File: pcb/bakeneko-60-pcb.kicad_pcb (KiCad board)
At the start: 2 copper layers, 284.7 x 94.2 mm, 151 parts, among them J1 JST SH 4-pin, J2 AVR-ISP-6, SW1 Reset, U1 SRV05-4, U2 ATmega32U4-AU, Y1 16MHz

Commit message: Update name/version
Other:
- board text added: "Unbakeneko60 v0.1"
- board text removed: "Bakeneko60 v3.0"
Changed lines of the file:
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@@
   (gr_line (start 284.7 91.95) (end 284.7 2.25) (layer "Edge.Cuts") (width 0.2))
   (gr_arc (start 249.918072 0.806452) (mid 250.470392 0.217362) (end 251.248106 0) (layer "Edge.Cuts") (width 0.2))
-  (gr_text "Bakeneko60 v3.0" (at 274.915477 91.907501) (layer "B.SilkS")
+  (gr_text "Unbakeneko60 v0.1" (at 274.915477 91.907501) (layer "B.SilkS")
     (effects (font (size 1 1) (thickness 0.15)) (justify mirror))
   )

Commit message: Renumbering and cleanup
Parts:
- added D59: 1N4148, Diode_SMD:D_SOD-123, B.Cu at (82.8, 86.0)
- added D60: 1N4148, Diode_SMD:D_SOD-123, B.Cu at (116.1, 86.0)
- added D61: 1N4148, Diode_SMD:D_SOD-123, B.Cu at (154.3, 86.0)
- renumbered D60 to D62, D61 to D63, D62 to D64, D63 to D65
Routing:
- net Net-(D58-Pad2): track 6.82 -> 27.3 mm
- net COL11: track 295.1 -> 292.8 mm

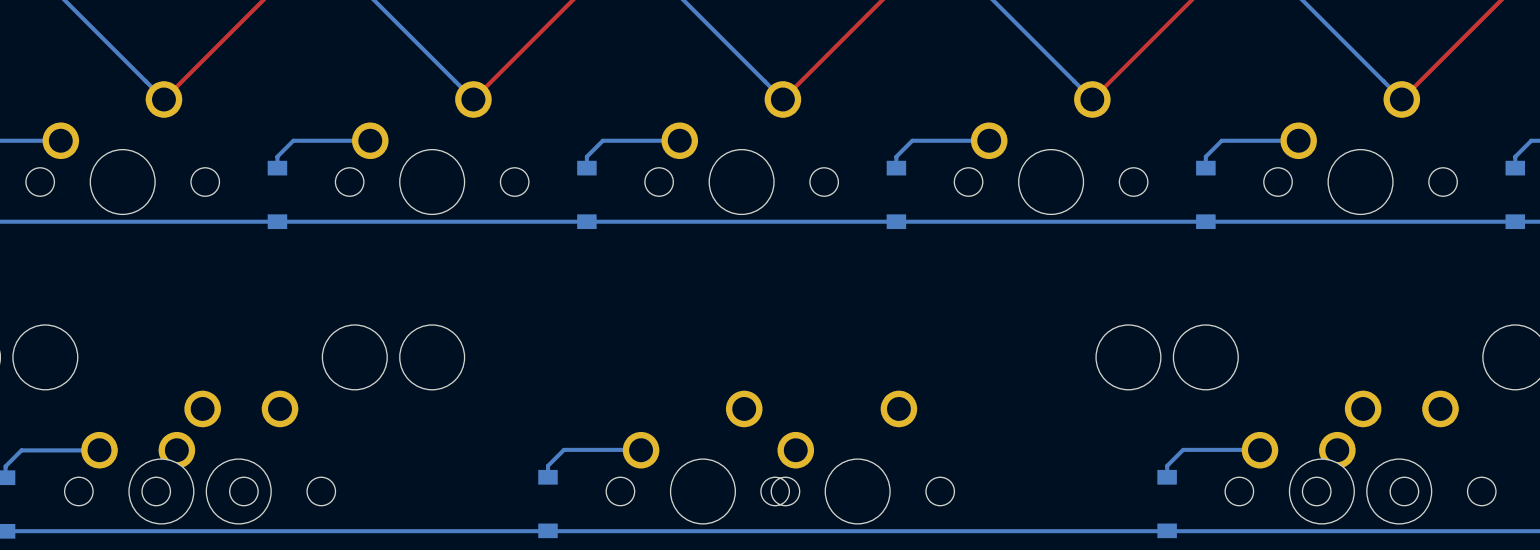
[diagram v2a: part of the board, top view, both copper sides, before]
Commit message: Add remaining traces
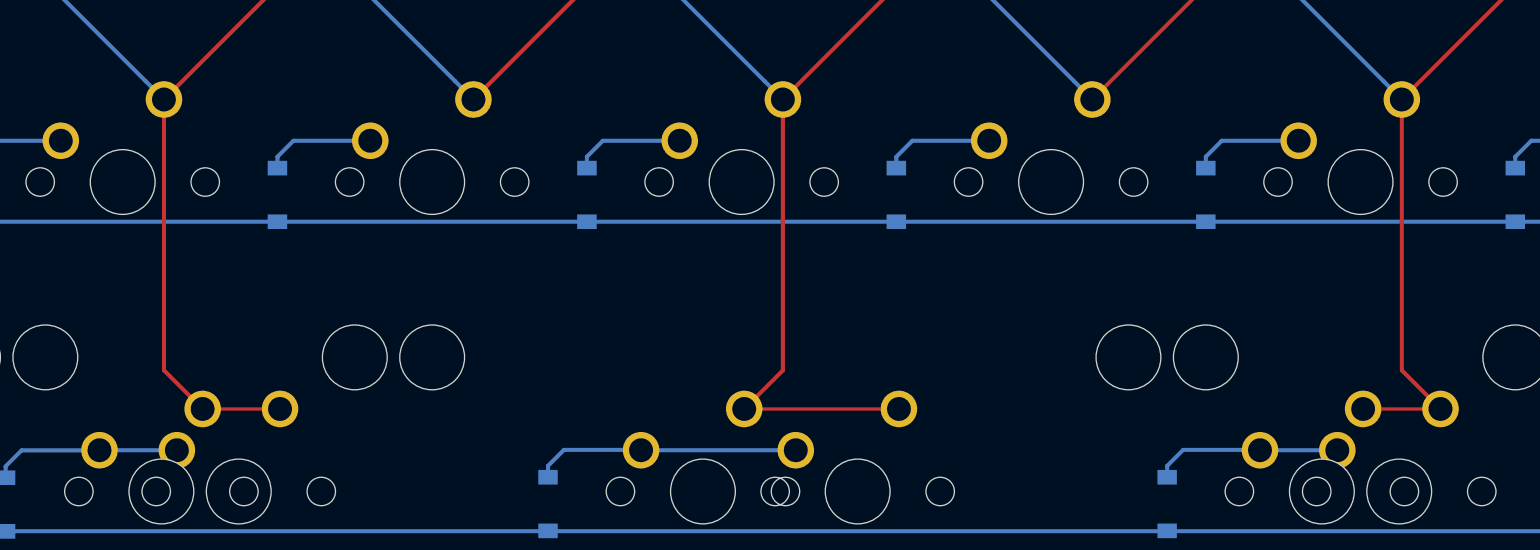
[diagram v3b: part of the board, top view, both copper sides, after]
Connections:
- D59 pad 2: Net-(D58-Pad2) -> Net-(D59-Pad2)
- D60 pad 2: Net-(D58-Pad2) -> Net-(D60-Pad2)
- D61 pad 2: Net-(D58-Pad2) -> Net-(D61-Pad2)
- MX62 pad 1: (no net) -> Net-(D59-Pad2)
- MX62 pad 2: (no net) -> COL4
- MX63 pad 2: (no net) -> COL4
- MX64 pad 1: (no net) -> Net-(D60-Pad2)
- MX64 pad 2: (no net) -> COL6
- MX65 pad 2: (no net) -> COL6
- MX66 pad 1: (no net) -> Net-(D61-Pad2)
- MX66 pad 2: (no net) -> COL8
- MX67 pad 1: (no net) -> Net-(D61-Pad2)
- MX67 pad 2: (no net) -> COL8
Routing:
- net COL6: track 180.1 -> 209.7 mm
- net COL8: track 217.4 -> 242.2 mm
- net COL4: track 143.4 -> 168.2 mm
- net Net-(D58-Pad2): track 27.3 -> 6.82 mm
- net Net-(D60-Pad2): track 0.00 -> 16.3 mm
- net Net-(D59-Pad2): track 0.00 -> 11.6 mm
- net Net-(D61-Pad2): track 0.00 -> 11.6 mm

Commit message: Remove unconnected traces
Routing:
- net COL2: track 145.1 -> 144.2 mm
- net +5V: track 122.7 -> 121.9 mm
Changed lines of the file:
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@@
   (segment (start 22.85375 37.75875) (end 21.85375 37.75875) (width 0.25) (layer "B.Cu") (net 54))
   (segment (start 21.85375 37.75875) (end 20.508769 36.413769) (width 0.25) (layer "B.Cu") (net 54))
-  (segment (start 266.1375 68.59375) (end 266.14375 68.6) (width 0.25) (layer "B.Cu") (net 54))
   (segment (start 28.84375 68.59375) (end 266.1375 68.59375) (width 0.25) (layer "B.Cu") (net 54))
   (segment (start 119.52125 63.61) (end 118.5375 64.59375) (width 0.25) (layer "B.Cu") (net 55))
@@
   (segment (start 45.1 17) (end 44.225 17) (width 0.2) (layer "B.Cu") (net 73))
   (segment (start 41.540001 17.275) (end 43.85 17.275) (width 0.2) (layer "B.Cu") (net 73))
-  (segment (start 24.80375 14.040002) (end 24.82375 14.020002) (width 0.25) (layer "F.Cu") (net 74))
   (segment (start 24.71 20.922661) (end 24.71 14.020002) (width 0.25) (layer "F.Cu") (net 74))
   (segment (start 31.902295 22.228536) (end 31.403751 21.729992) (width 0.25) (layer "F.Cu") (net 74))
@@
   (segment (start 23.100031 13.660033) (end 14.175959 13.660033) (width 0.25) (layer "B.Cu") (net 75))
   (segment (start 25.20375 14.78) (end 25.560001 14.423749) (width 0.25) (layer "F.Cu") (net 76))
-  (segment (start 33.152295 23.252418) (end 33.15375 23.250963) (width 0.25) (layer "F.Cu") (net 76))
   (segment (start 33.152295 21.928545) (end 32.503731 21.279981) (width 0.25) (layer "F.Cu") (net 76))
   (segment (start 32.503731 21.279981) (end 25.703731 21.279981) (width 0.25) (layer "F.Cu") (net 76))
@@
   (segment (start 13.92125 42.02) (end 13.92125 38.638765) (width 0.25) (layer "F.Cu") (net 77))
   (segment (start 24.643741 59.872509) (end 24.643741 51.179221) (width 0.25) (layer "F.Cu") (net 77))
-  (segment (start 15.58224 80.05) (end 15.68734 80.05) (width 0.25) (layer "F.Cu") (net 77))
   (segment (start 22.684345 46.020595) (end 22.684345 47.640595) (width 0.25) (layer "F.Cu") (net 77))
   (segment (start 13.92125 38.638765) (end 16.3025 36.257515) (width 0.25) (layer "F.Cu") (net 77))
-  (segment (start 15.51224 80.12) (end 15.58224 80.05) (width 0.25) (layer "F.Cu") (net 77))
   (segment (start 23.44625 61.07) (end 24.643741 59.872509) (width 0.25) (layer "F.Cu") (net 77))
   (segment (start 18.68375 42.02) (end 22.684345 46.020595) (width 0.25) (layer "F.Cu") (net 77))
@@
   (segment (start 39.295 22.15) (end 40.115 22.97) (width 0.25) (layer "B.Cu") (net 78))
   (segment (start 30.15375 32.05875) (end 30.15375 29.60298) (width 0.25) (layer "B.Cu") (net 78))
-  (segment (start 21.23377 36.96593) (end 21.23377 37.34002) (width 0.25) (layer "F.Cu") (net 79))
   (segment (start 26.24875 49.95) (end 25.32375 49.95) (width 0.25) (layer "F.Cu") (net 79))
   (segment (start 49.64 3.92) (end 49.64 13.445) (width 0.25) (layer "F.Cu") (net 79))
@@
   (segment (start 26.24875 49.95) (end 26.645716 49.95) (width 0.25) (layer "B.Cu") (net 79))
   (segment (start 49.051383 55.718883) (end 49.501389 56.168889) (width 0.25) (layer "B.Cu") (net 79))
-  (segment (start 35.29375 55.72) (end 35.86375 55.72) (width 0.25) (layer "B.Cu") (net 79))
   (segment (start 22.85375 36.95875) (end 21.85375 36.95875) (width 0.25) (layer "B.Cu") (net 79))
   (segment (start 29.908317 53.212605) (end 32.786355 53.212605) (width 0.25) (layer "B.Cu") (net 79))
@@
   (segment (start 16.23625 39.35875) (end 16.6475 39.77) (width 0.381) (layer "B.Cu") (net 94))
   (segment (start 38.179381 31.459383) (end 37.779382 31.859382) (width 0.381) (layer "B.Cu") (net 94))
-  (segment (start 12.604391 15.960641) (end 12.804524 15.760509) (width 0.381) (layer "B.Cu") (net 94))
   (segment (start 36.36 32.9825) (end 36.05551 33.28699) (width 0.381) (layer "B.Cu") (net 94))
   (segment (start 14.366043 14.198989) (end 21.388989 14.198989) (width 0.381) (layer "B.Cu") (net 94))
   (segment (start 12.604391 15.960641) (end 14.366043 14.198989) (width 0.381) (layer "B.Cu") (net 94))
   (segment (start 31.1225 48.2575) (end 31.12 48.26) (width 0.381) (layer "B.Cu") (net 94))
-  (segment (start 31.853749 43.558749) (end 31.75375 43.45875) (width 0.381) (layer "B.Cu") (net 94))
   (segment (start 35.180291 35.35875) (end 34.25375 35.35875) (width 0.381) (layer "B.Cu") (net 94))
   (segment (start 23.31 27.19875) (end 24.06125 27.95) (width 0.381) (layer "B.Cu") (net 94))
@@
   (segment (start 22.85375 33.75875) (end 22.85375 32.081002) (width 0.381) (layer "B.Cu") (net 94))
   (segment (start 31.1225 46.91) (end 31.1225 48.2575) (width 0.381) (layer "B.Cu") (net 94))
-  (segment (start 16.23625 38.55875) (end 16.49 38.8125) (width 0.381) (layer "B.Cu") (net 94))
   (segment (start 16.6475 39.77) (end 19.468328 39.77) (width 0.381) (layer "B.Cu") (net 94))
   (segment (start 16.598835 37.25548) (end 17.16452 37.25548) (width 0.381) (layer "B.Cu") (net 94))
@@
   (segment (start 26.15375 30.933749) (end 26.15375 32.05875) (width 0.2) (layer "B.Cu") (net 96))
   (segment (start 28.33305 17.275) (end 26.32875 19.2793) (width 0.2) (layer "B.Cu") (net 96))
-  (segment (start 26.33375 28.17195) (end 26.32875 28.17695) (width 0.2) (layer "B.Cu") (net 96))
   (segment (start 26.32875 19.2793) (end 26.32875 28.17695) (width 0.2) (layer "B.Cu") (net 96))
   (segment (start 29.299963 27.712463) (end 29.299963 29.282035) (width 0.25) (layer "B.Cu") (net 98))
@@
   (segment (start 42.55375 14.7) (end 42.55375 24.71) (width 0.25) (layer "F.Cu") (net 100))
   (segment (start 42.55375 24.71) (end 49.204145 31.360395) (width 0.25) (layer "F.Cu") (net 100))
-  (segment (start 49.204145 32.139605) (end 49.204145 32.239605) (width 0.25) (layer "F.Cu") (net 100))
   (segment (start 42.55375 14.505703) (end 42.55375 14.7) (width 0.25) (layer "F.Cu") (net 100))
   (via (at 42.55375 14.020002) (size 0.8) (drill 0.4) (layers "F.Cu" "B.Cu") (net 100))
@@
   (zone (net 1) (net_name "GND") (layer "B.Cu") (hatch edge 0.508)
     (connect_pads (clearance 0.254))
-    (min_thickness 0.254)
+    (min_thickness 0.254) (filled_areas_thickness no)
     (fill yes (thermal_gap 0.254) (thermal_bridge_width 0.381))
     (polygon
@@
   (zone (net 1) (net_name "GND") (layer "B.Cu") (hatch edge 0.508)
     (connect_pads (clearance 0.508))
-    (min_thickness 0.254)
+    (min_thickness 0.254) (filled_areas_thickness no)
     (fill yes (thermal_gap 0.508) (thermal_bridge_width 0.508))
     (polygon
